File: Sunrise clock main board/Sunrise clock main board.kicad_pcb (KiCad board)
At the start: 2 copper layers, 160 x 106.7 mm, 142 parts, among them J1 Barrel_Jack_Switch, J2 Screw terminal/dnf, J3 Screw terminal/dnf, J4 Conn_02x05_Odd_Even, J5 Conn_01x04_Male, J6 Conn_01x04_Male, J7 Conn_01x05_Male, Q2 IRML2244, SW1 SW_Push, SW2 SW_Push, SW3 SW_Push, SW4 SW_Push, SW5 SW_Push, SW6 SW_Push, SW7 SW_Push, SW8 SW_Push, U1 NCP1117LPST33T3G, U10 74HC138D, U2 MAX809S, U3 LM258DR, U4 DS3231MZ, U5 AT24C32N, U6 PCA9306DCTR, U7 74AHC125D, U8 74HC4066D, U9 MCP23017_SP

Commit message: Tweaks
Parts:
- F1, F2: footprint Fuse:Fuse_1812_4532Metric_Pad1.30x3.40mm_HandSolder -> Fuse-fixed:Fuse_1812_4532Metric_Pad1.30x3.40mm_HandSolder
- L1: footprint Inductor-extra:L_12x12mm_H8mm-L_Radial_D10.0mm_P5.00mm -> Inductor-fixed:L_12x12mm_H8mm
- U3: value LM258DR -> LM358DR; footprint Package_SO-extra:Dual_SO-8_3.9x4.9mm_P1.27mm+DIP8 -> Package_SO:SOIC-8_3.9x4.9mm_P1.27mm
- renumbered C27 to C14, C14 to C6
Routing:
- net +BATT: track 45.4 -> 40.9 mm
- net Net-(C3-Pad1): track 27.9 -> 24.4 mm
- net /Power/RC_NEO_GND: track 26.8 -> 24.8 mm, vias 0 -> 1
- net GND2: track 117.7 -> 119.5 mm, vias 2 -> 3
- net +5V: track 688.0 -> 686.8 mm
- net EXP_INT: track 56.2 -> 55.1 mm
- net GPA5: track 29.4 -> 30.6 mm
- net Net-(R29-Pad2): track 14.2 -> 15.1 mm
- net ~RESET_5V: track 25.3 -> 24.6 mm
- net Net-(Q2-Pad1): track 126.8 -> 127.6 mm
- net +3V3: track 398.3 -> 397.6 mm
- net Net-(R30-Pad1): track 20.0 -> 19.5 mm
- net GPA2: track 63.0 -> 62.4 mm
- net Net-(R13-Pad2): track 27.0 -> 26.6 mm, vias 1 -> 2
- net GND: vias 99 -> 102

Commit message: Now in stereo if you want.
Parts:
- removed C19, C20, C21, C22, C23, C24, C25, C26: 100nF, Capacitor_SMD:C_0805_2012Metric_Pad1.18x1.45mm_HandSolder
- removed F5: Polyfuse 250mA >=6V, Fuse:Fuse_1206_3216Metric_Pad1.42x1.75mm_HandSolder
- removed J2: Screw terminal/dnf, TerminalBlock_Phoenix:TerminalBlock_Phoenix_MKDS-1,5-2-5.08_1x02_P5.08mm_Horizontal
- removed J7: Conn_01x05_Male, Connector_PinHeader_2.54mm:PinHeader_1x05_P2.54mm_Vertical
- removed R21, R22, R23, R24, R25, R26, R27, R28: 1k, Resistor_SMD:R_0805_2012Metric_Pad1.20x1.40mm_HandSolder
- removed R52, R53, R54, R55, R56, R57, R58, R59: 100k, Resistor_SMD:R_0805_2012Metric_Pad1.20x1.40mm_HandSolder
- removed the R63 at (-27.9, 14.0)
- added A4: max98357, Module-extra:max98357, F.Cu at (10.2, 16.5)
- added D5: BAV99, Package_TO_SOT_SMD:SOT-23, F.Cu at (31.8, -39.4)
- added D6: BAV99, Package_TO_SOT_SMD:SOT-23, F.Cu at (27.9, -39.4)
- added LOGO1: Logo_Open_Hardware_Large, Symbol:OSHW-Logo_11.4x12mm_SilkScreen, F.Cu at (0.00, -10.2)
- added Q1: IRML2244, Package_TO_SOT_SMD:SOT-23, F.Cu at (31.8, -33.0)
- added Q3: 2N7002, Package_TO_SOT_SMD:SOT-23, F.Cu at (-12.7, 15.2)
- added Q4: 2N7002, Package_TO_SOT_SMD:SOT-23, F.Cu at (8.89, 16.5)
- added R14: 100R, Resistor_SMD:R_0805_2012Metric_Pad1.20x1.40mm_HandSolder, F.Cu at (-22.9, 14.0)
- added R16: 100R, Resistor_SMD:R_0805_2012Metric_Pad1.20x1.40mm_HandSolder, F.Cu at (-20.3, 14.0)
- added R66: 100k, Resistor_SMD:R_0805_2012Metric_Pad1.20x1.40mm_HandSolder, F.Cu at (27.9, -33.0)
- added R67: 100k, Resistor_SMD:R_0805_2012Metric_Pad1.20x1.40mm_HandSolder, F.Cu at (-77.5, 20.3)
- added R68: 100k, Resistor_SMD:R_0805_2012Metric_Pad1.20x1.40mm_HandSolder, F.Cu at (-47.0, 31.8)
- added R69: 100k, Resistor_SMD:R_0805_2012Metric_Pad1.20x1.40mm_HandSolder, F.Cu at (5.08, 21.6)
- added R70: 100k, Resistor_SMD:R_0805_2012Metric_Pad1.20x1.40mm_HandSolder, F.Cu at (3.81, 15.2)
- added R71: 100k, Resistor_SMD:R_0805_2012Metric_Pad1.20x1.40mm_HandSolder, F.Cu at (-25.4, 14.0)
- added R79: 560k, Resistor_SMD:R_0805_2012Metric_Pad1.20x1.40mm_HandSolder, F.Cu at (14.0, 15.2)
- added TP18: TestPoint, TestPoint:TestPoint_THTPad_1.5x1.5mm_Drill0.7mm, F.Cu at (-24.8, 7.62)
- added TP19: TestPoint, TestPoint:TestPoint_THTPad_1.5x1.5mm_Drill0.7mm, F.Cu at (73.9, -23.6)
- added TP20: TestPoint, TestPoint:TestPoint_THTPad_1.5x1.5mm_Drill0.7mm, F.Cu at (-52.1, 19.1)
- J3: footprint TerminalBlock_Phoenix:TerminalBlock_Phoenix_MKDS-1,5-3-5.08_1x03_P5.08mm_Horizontal -> TerminalBlock_Phoenix:TerminalBlock_Phoenix_MKDS-1,5-5-5.08_1x05_P5.08mm_Horizontal
- NT1: footprint NetTie:NetTie-2_SMD_Pad0.5mm -> NetTie-fixed:NetTie-2_SMD_Pad0.5mm; moved to F.Cu
- R63: renamed from R41; value 10k -> 100k
- U5: value AT24C32N -> AT24C512C-SSHD
- moved D4 25.4 mm to (20.3, -39.4), turned to 0 degrees
- moved R3 24.7 mm to (-29.2, 14.0)
- moved J3 14.8 mm to (11.4, -25.4)
- moved NT1 14.2 mm to (-1.27, -22.9), turned to 0 degrees
- moved R1 13.3 mm to (0.00, -22.9), turned to 0 degrees
- moved D3 10.9 mm to (24.1, -39.4)
- moved A3 10.2 mm to (-10.2, 16.5)
- moved R63 10.1 mm to (17.8, -33.0)
- moved R41 7.97 mm to (33.0, -48.3), turned to 0 degrees
- moved Q2 4.58 mm to (21.6, -33.0), turned to 270 degrees
- moved R62 3.81 mm to (-19.1, 20.3)
- renumbered A7 to A5, C40 to C33, R14 to R1, R1 to R15, R29 to R20, R47 to R41, R51 to R78, R70 to R80, R80 to R90
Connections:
- net /Power/RC_NEO_GND renamed Net-(C5-Pad1)
- net IO33 renamed GPIO33
- net IO5 renamed GPIO5
- net NEOPIXEL_GND renamed EXTERNAL_GND
- net NEOPIXEL_POWER renamed EXTERNAL_CURRENT
- A3 pad 4: I2S_GAIN -> I2S_GAIN0
- A3 pad 5: I2S_SD -> ~SDL
- A3 pad 8: /Output/SPK- -> Net-(A3-Pad8)
- A3 pad 9: /Output/SPK+ -> Net-(A3-Pad9)
- D3 pad 2: Net-(D3-Pad2) -> Net-(C3-Pad1)
- D4 pad 2: +5V -> Net-(C3-Pad1)
- F1 pad 1: Net-(D3-Pad2) -> Net-(C3-Pad1)
- F1 pad 2: Net-(C3-Pad1) -> Net-(F1-Pad2)
- L1 pad 2: Net-(C3-Pad1) -> Net-(F1-Pad2)
- Q2 pad 2: Net-(D3-Pad2) -> Net-(C3-Pad1)
- R3 pad 2: Net-(R3-Pad2) -> NEOPIXEL_~EN
- R62 pad 1: Net-(R62-Pad1) -> I2S_GAIN0
- R62 pad 2: I2S_GAIN -> I2S_GAIN1
- SW1 pad 1: Net-(R21-Pad1) -> GPA0
- SW2 pad 1: Net-(R22-Pad1) -> GPA1
- SW3 pad 1: Net-(R23-Pad1) -> GPA2
- SW4 pad 1: Net-(R24-Pad1) -> GPA3
- SW5 pad 1: Net-(R25-Pad1) -> GPA4
- SW6 pad 1: Net-(R26-Pad1) -> GPA5
- SW7 pad 1: Net-(R27-Pad1) -> GPA6
- SW8 pad 1: Net-(R28-Pad1) -> GPA7
- U7 pad 2: NEOPIXEL_~EN -> GND
- U7 pad 3: Net-(R3-Pad2) -> Net-(U7-Pad3)
- U9 pad 1: /Control/GPB0 -> GPIO1
- U9 pad 2: /Control/GPB1 -> GPO2
- U9 pad 3: /Control/GPB2 -> Net-(TP18-Pad1)
- U9 pad 6: I2S_GAIN -> I2S_GAIN0
- U9 pad 7: Net-(R62-Pad1) -> I2S_GAIN1
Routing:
- net +5V: track 686.8 -> 500.1 mm, vias 11 -> 16
- net Net-(Q1-Pad1): track 0.00 -> 102.9 mm, vias 0 -> 2
- net Net-(D6-Pad3): track 0.00 -> 100.7 mm, vias 0 -> 3
- net I2S_GAIN0: track 0.00 -> 72.3 mm, vias 0 -> 2
- net I2S_GAIN: track 45.5 -> 0.00 mm, vias 1 -> 0
- net I2S_GAIN1: track 0.00 -> 42.4 mm
- net NEOPIXEL_~EN: track 35.8 -> 7.05 mm, vias 2 -> 0
- net Net-(Q2-Pad1): track 127.6 -> 101.6 mm
- net ~SDL: track 0.00 -> 24.8 mm, vias 0 -> 1
- net Net-(D3-Pad2): track 24.4 -> 0.00 mm
- net /Output/SPK+: track 20.7 -> 0.00 mm
- net GPA6: track 67.9 -> 87.6 mm, vias 2 -> 1
- net GPA7: track 78.1 -> 97.7 mm, vias 2 -> 1
- net GPA2: track 62.4 -> 80.9 mm, vias 2 -> 1
- net Net-(C3-Pad1): track 24.4 -> 42.2 mm
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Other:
- board text added: "+"
- board text added: "-"
- board text added: "2: Neopixel data"
- board text added: "3: Neopixel 5V"
- board text added: "4: GPIO"
- board text added: "5: GPO 5V"
- board text added: "CR2032 coin cell"
- board text added: "Do not fit any components in this square if you want only mono output."
- board text added: "I2C: 0x50 EEPROM"
- board text added: "I2C: 0x76 BME280"
- board text added: "IO expander"
- board text added: "MEMS RTC"
- board text added: "Sunrise clock V1.0, 2021-04-10 https://github.com/atoomnetmarc/Sunrise-clock-hardware Apache License, Version 2.0"
- board text added: "left or mono"
- board text added: "right"
- board text removed: "+ -"
- board text removed: "2: DOUT"
- board text removed: "3: 5V"
- board text removed: "3W speaker"
- board text removed: "CR2032"
- board text removed: "GPB0"
- board text removed: "GPB1"
- board text removed: "GPIO"
- board text removed: "I2C: 0x50"
- board text removed: "I2C: 0x76"
- board text removed: "Neopixel"
- board text removed: "Sunrise clock V1.0, 2021-04-09 https://github.com/atoomnetmarc/Sunrise-clock-hardware Apache License, Version 2.0"

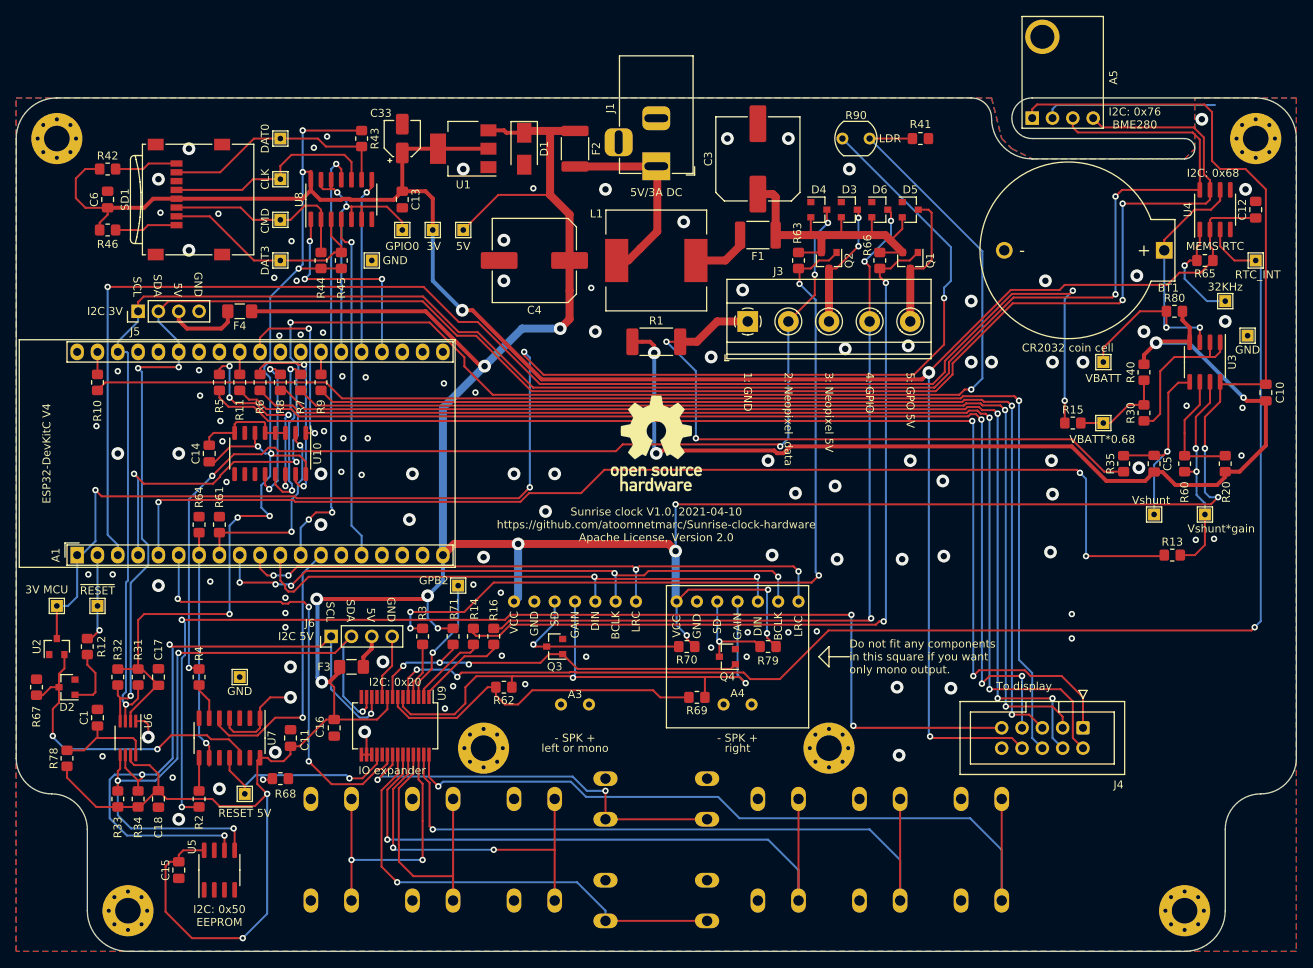
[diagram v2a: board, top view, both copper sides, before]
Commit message: Added gerbers and bom.
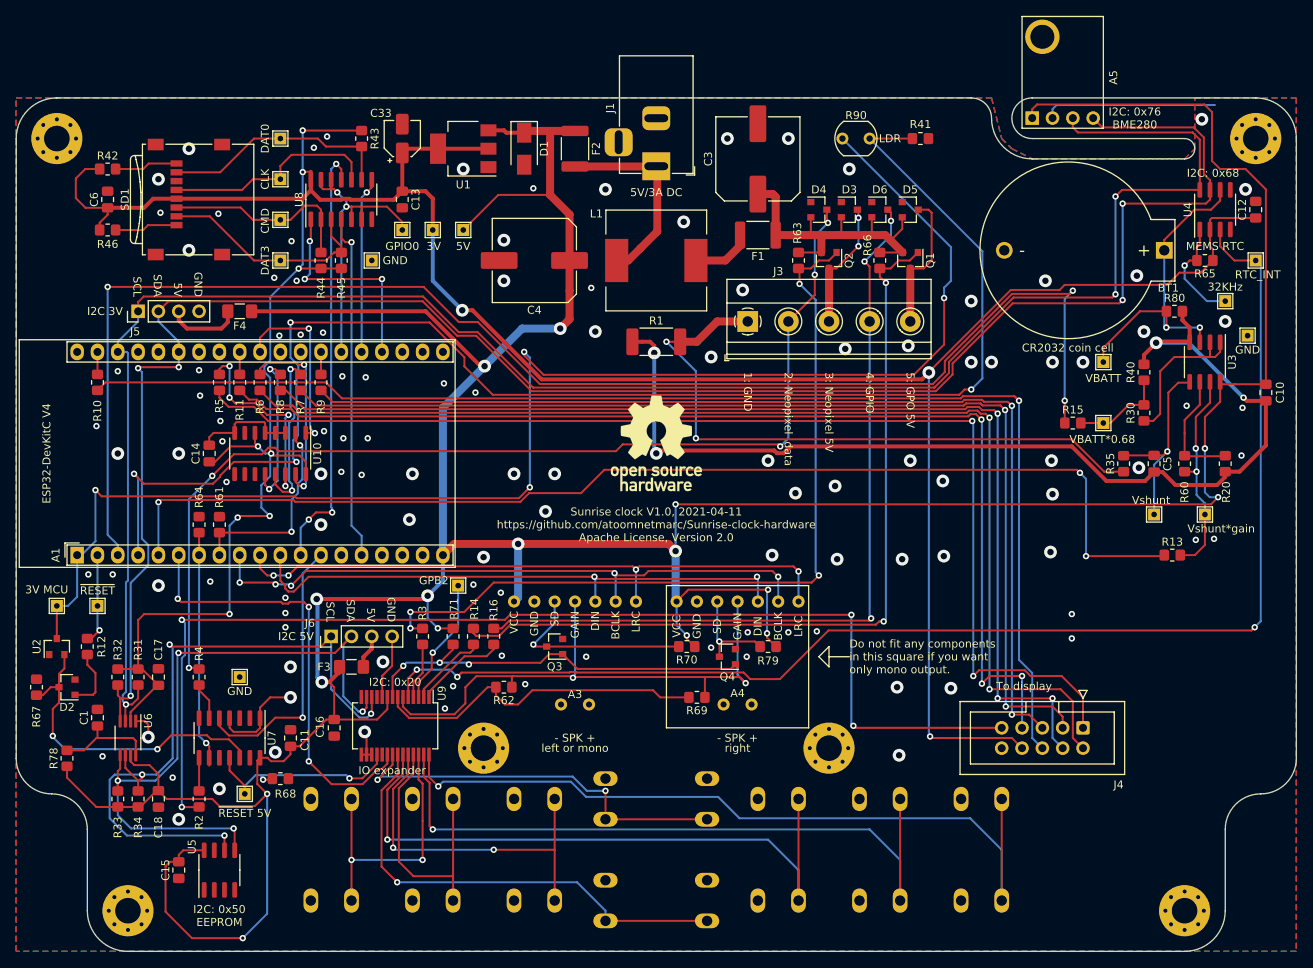
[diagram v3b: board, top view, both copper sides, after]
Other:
- board text added: "Sunrise clock V1.0, 2021-04-11 https://github.com/atoomnetmarc/Sunrise-clock-hardware Apache License, Version 2.0"
- board text removed: "Sunrise clock V1.0, 2021-04-10 https://github.com/atoomnetmarc/Sunrise-clock-hardware Apache License, Version 2.0"

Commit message: Start of V1.1
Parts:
- removed C18: 100nF, Capacitor_SMD:C_0805_2012Metric_Pad1.18x1.45mm_HandSolder
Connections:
- U6 pad 7: +5V -> Net-(C1-Pad1)
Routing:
- net +5V: track 500.1 -> 492.2 mm
- net Net-(C1-Pad1): track 12.6 -> 16.5 mm
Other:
- board text added: "Sunrise clock V1.1, 2021-05-02 https://github.com/atoomnetmarc/Sunrise-clock-hardware Apache License, Version 2.0"
- board text removed: "Sunrise clock V1.0, 2021-04-11 https://github.com/atoomnetmarc/Sunrise-clock-hardware Apache License, Version 2.0"

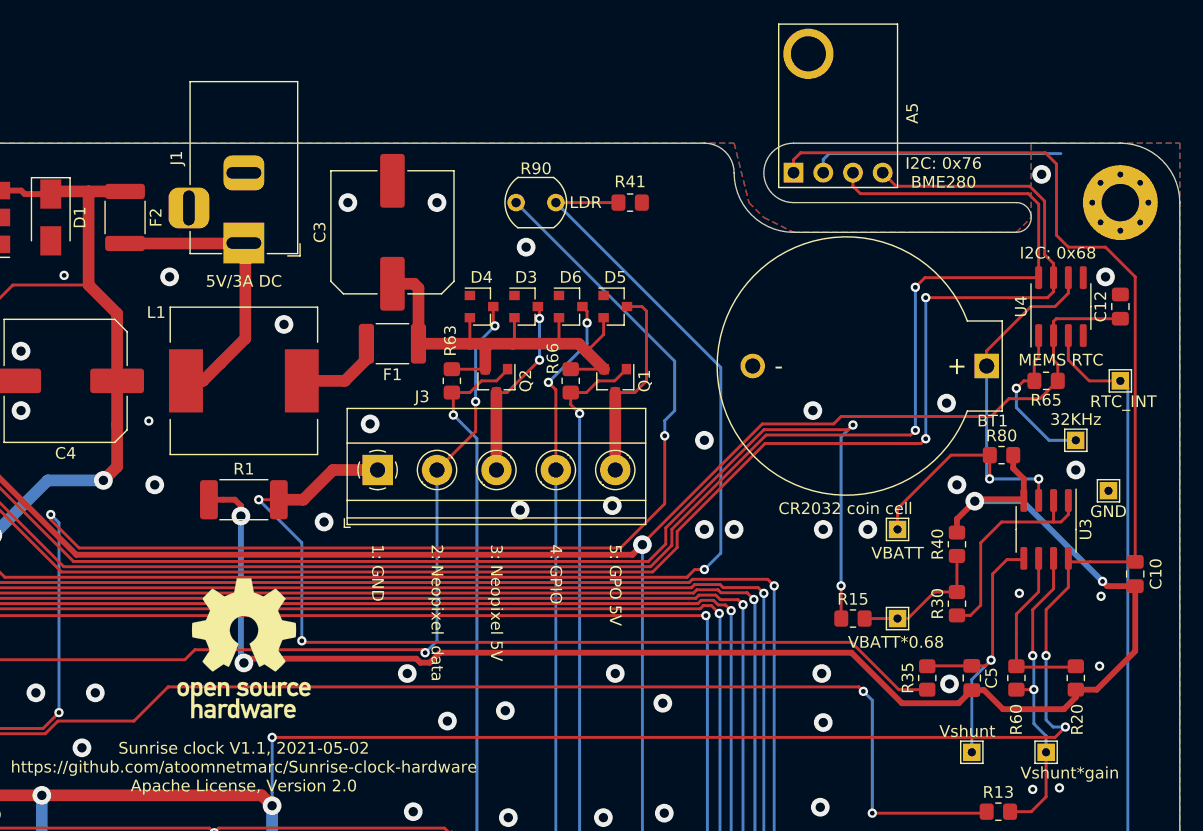
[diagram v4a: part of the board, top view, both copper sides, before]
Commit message: changed BME280 module to a 3v one
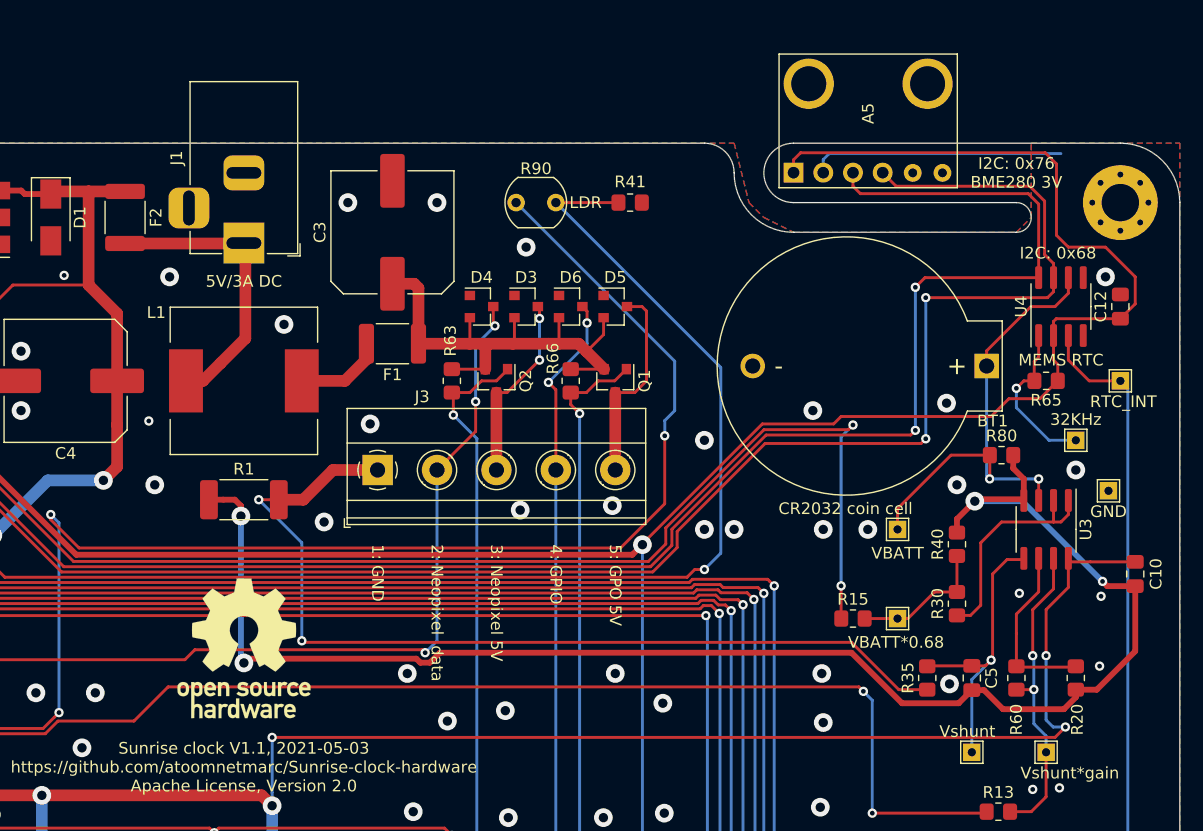
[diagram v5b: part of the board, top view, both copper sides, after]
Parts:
- A5: value BME280 module -> BME280 module 3V; footprint Module-extra:bme280 -> Module-extra:bme280_3V
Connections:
- A5 pad 1: +5V -> +3V3
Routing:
- net +5V: track 492.2 -> 429.3 mm
- net +3V3: track 391.3 -> 433.9 mm
- net GND: vias 117 -> 116
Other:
- board text added: "I2C: 0x76 BME280 3V"
- board text added: "Sunrise clock V1.1, 2021-05-03 https://github.com/atoomnetmarc/Sunrise-clock-hardware Apache License, Version 2.0"
- board text removed: "I2C: 0x76 BME280"
- board text removed: "Sunrise clock V1.1, 2021-05-02 https://github.com/atoomnetmarc/Sunrise-clock-hardware Apache License, Version 2.0"

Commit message: Started with checklist.
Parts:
- U7: value 74AHC125D -> 74AHCT125D
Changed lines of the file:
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@@
       (effects (font (size 1 1) (thickness 0.15)))
     )
-    (fp_text value 74AHC125D (at 0 5.28 90) (layer F.Fab)
+    (fp_text value 74AHCT125D (at 0 5.28 90) (layer F.Fab)
       (effects (font (size 1 1) (thickness 0.15)))
     )
